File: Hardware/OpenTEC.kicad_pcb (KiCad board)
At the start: 4 copper layers, 130 x 90 mm, 67 parts, among them J10 TEMP3, J11 TEC, J12 XH2.54, J13 XH2.54, J14 XH2.54, J15 XH2.54, J16 XH2.54, J17 XH2.54, J18 XH2.54, J19 XH2.54, J2 4P Screw Terminal, J20 XH2.54, J21 XH2.54, J22 XH2.54, J23 XH2.54, J24 XH2.54, J25 XH2.54, J26 XH2.54, J27 XH2.54, J3 10P JTAG/SWD, J4 LCD, J5 I2C, J6 BOOT_SEL, J7 TEMP0, J8 TEMP1, J9 TEMP2, Q1 FDS6574A, Q2 FDS6574A, Q3 FDS6574A, Q4 FDS6574A, U11 STM32F103C8T6, U2 AMS1117-3.3, U3 IR2104, U4 IR2104, Y1 16MHz

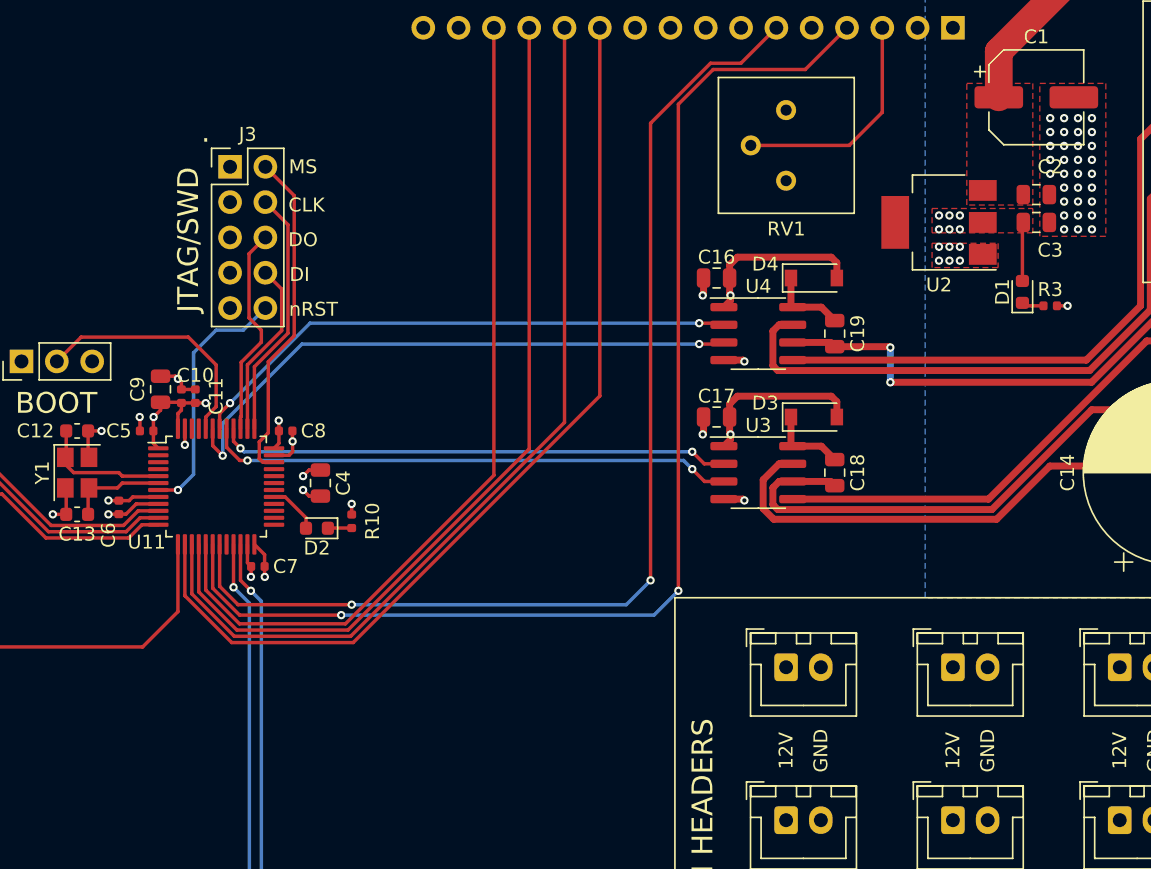
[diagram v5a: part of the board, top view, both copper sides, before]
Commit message: Add control push buttons
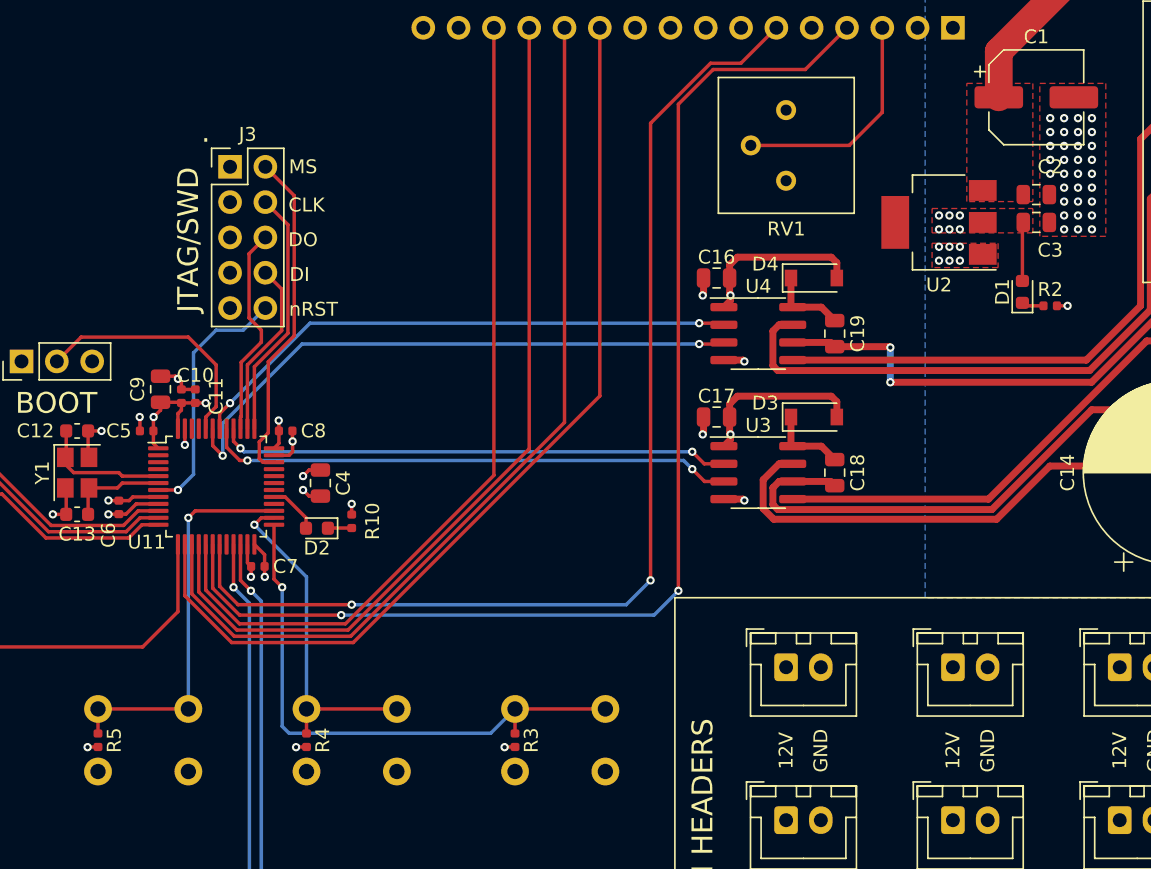
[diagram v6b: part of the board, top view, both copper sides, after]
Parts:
- added R3: 2.2K, Resistor_SMD:R_0402_1005Metric, F.Cu at (124.5, 112.2)
- added R4: 2.2K, Resistor_SMD:R_0402_1005Metric, F.Cu at (109.5, 112.2)
- added R5: 2.2K, Resistor_SMD:R_0402_1005Metric, F.Cu at (94.5, 112.2)
- added SW1: SW_Left, Button_Switch_THT:SW_PUSH_6mm, B.Cu at (131.0, 110.0)
- added SW2: SW_Mid, Button_Switch_THT:SW_PUSH_6mm, B.Cu at (116.0, 110.0)
- added SW3: SW_Right, Button_Switch_THT:SW_PUSH_6mm, B.Cu at (101.0, 110.0)
- renumbered R3 to R2
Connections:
- U11 pad 25: Net-(U11-Pad25) -> SW_Left
- U11 pad 26: Net-(U11-Pad26) -> SW_Mid
- U11 pad 27: Net-(U11-Pad27) -> SW_Right
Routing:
- net SW_Left: track 0.00 -> 40.7 mm, vias 0 -> 1
- net SW_Right: track 0.00 -> 28.4 mm, vias 0 -> 1
- net SW_Mid: track 0.00 -> 24.7 mm, vias 0 -> 1
- net GND: track 28.8 -> 31.1 mm, vias 95 -> 98

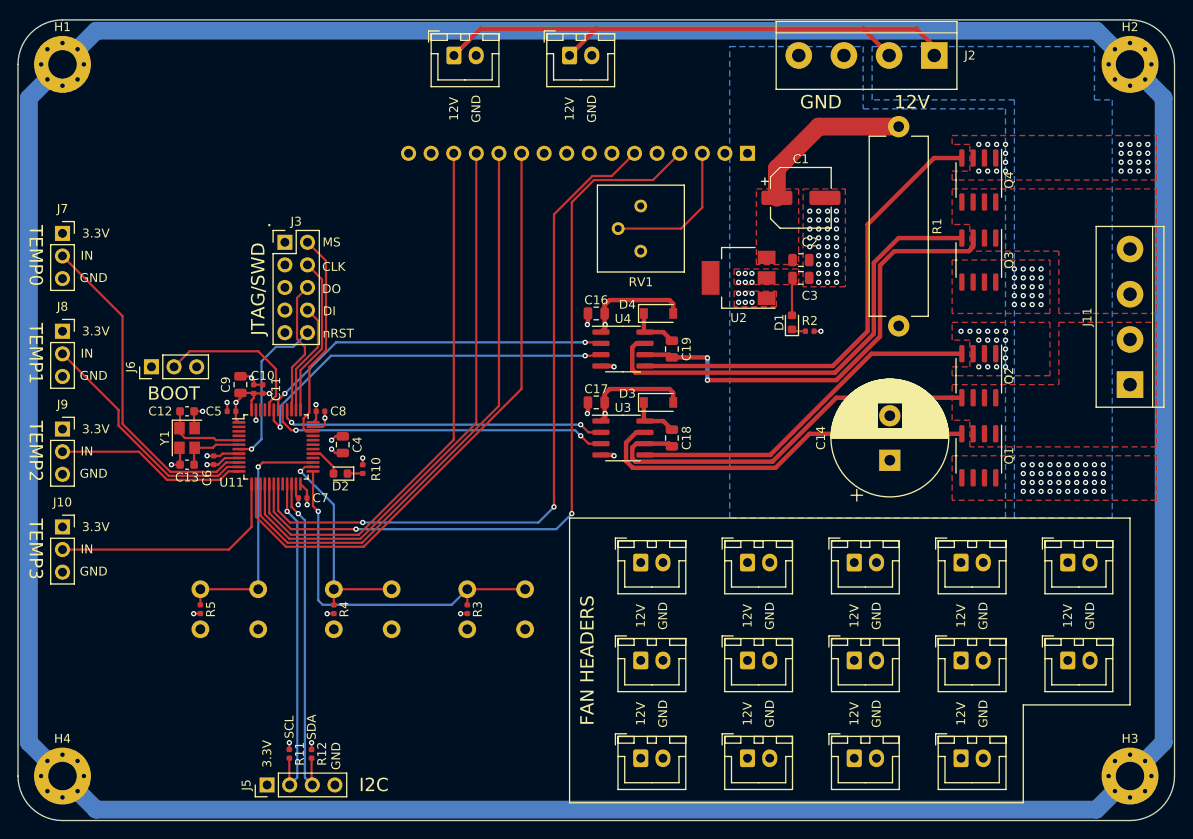
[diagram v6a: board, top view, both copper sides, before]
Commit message: Fix H-bridge supply voltage
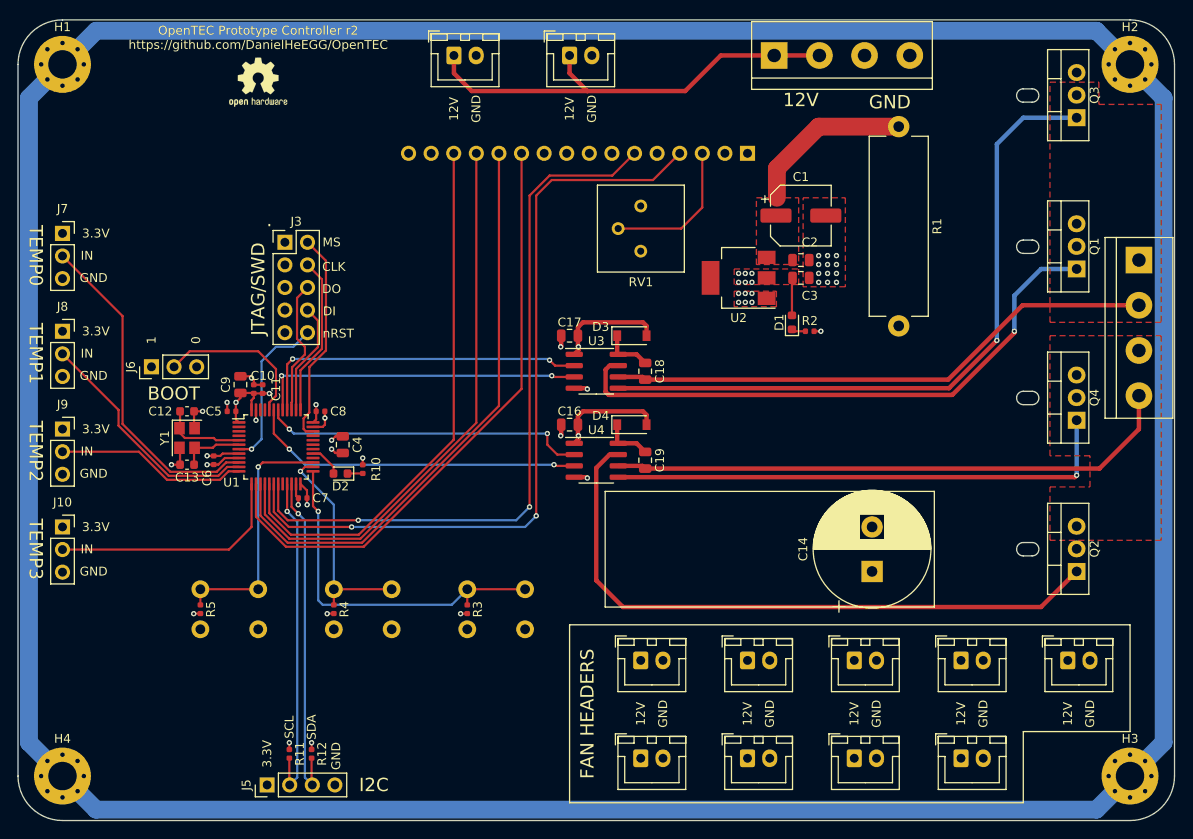
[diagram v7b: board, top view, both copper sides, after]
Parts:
- removed J23, J24, J25, J26, J27: XH2.54, Connector_JST:JST_XH_B2B-XH-A_1x02_P2.50mm_Vertical
- added REF**: OSHW-Logo2_7.3x6mm_SilkScreen, Symbol:OSHW-Logo2_7.3x6mm_SilkScreen, F.Cu at (101.0, 53.0)
- C1: footprint Capacitor_SMD:CP_Elec_6.3x5.8 -> Capacitor_SMD:CP_Elec_6.3x5.3
- Q1, Q2, Q3, Q4: value FDS6574A -> IRL2703; footprint Package_SO:SOIC-8_3.9x4.9mm_P1.27mm -> Package_TO_SOT_THT:TO-220-3_Vertical
- moved J12 97.4 mm to (123.0, 50.0)
- moved J14 68.5 mm to (144.0, 118.0)
- moved J19 52.8 mm to (144.0, 129.0)
- moved Q4 29.2 mm to (193.0, 91.0), turned to 90 degrees
- moved Q2 24.6 mm to (193.0, 108.0), turned to 90 degrees
- moved Q1 23.7 mm to (193.0, 74.0), turned to 90 degrees
- moved Q3 19.4 mm to (193.0, 57.0), turned to 90 degrees
- moved J2 18.0 mm to (159.0, 50.0), turned to 0 degrees
- moved J15 16.3 mm to (156.0, 118.0)
- moved J16 16.3 mm to (168.0, 118.0)
- moved J17 16.3 mm to (180.0, 118.0)
- moved J18 16.3 mm to (192.0, 118.0)
- moved J20 16.3 mm to (156.0, 129.0)
- moved J21 16.3 mm to (168.0, 129.0)
- moved J22 16.3 mm to (180.0, 129.0)
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- renumbered U11 to U1
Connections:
- C16 pad 1: +3V3 -> +12V
- C17 pad 1: +3V3 -> +12V
- D3 pad 2: +3V3 -> +12V
- D4 pad 2: +3V3 -> +12V
- Q1 pad 1: Net-(C18-Pad2) -> Net-(Q1-Pad1)
- Q1 pad 2: Net-(C18-Pad2) -> +12V
- Q2 pad 1: GND -> Net-(Q2-Pad1)
- Q2 pad 2: GND -> +12V
- Q2 pad 3: GND -> Net-(C19-Pad2)
- Q3 pad 1: Net-(C19-Pad2) -> Net-(Q3-Pad1)
- Q3 pad 2: Net-(C19-Pad2) -> Net-(C18-Pad2)
- Q3 pad 3: Net-(C19-Pad2) -> GND
- Q4 pad 1: GND -> Net-(Q4-Pad1)
- Q4 pad 2: GND -> Net-(C19-Pad2)
- U3 pad 1: +3V3 -> +12V
- U3 pad 5: Net-(Q2-Pad4) -> Net-(Q3-Pad1)
- U3 pad 7: Net-(Q1-Pad4) -> Net-(Q1-Pad1)
- U4 pad 1: +3V3 -> +12V
- U4 pad 5: Net-(Q4-Pad4) -> Net-(Q4-Pad1)
- U4 pad 7: Net-(Q3-Pad4) -> Net-(Q2-Pad1)
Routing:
- net Net-(Q3-Pad1): track 0.00 -> 77.0 mm, vias 0 -> 1
- net Net-(Q2-Pad1): track 0.00 -> 72.6 mm
- net Net-(Q1-Pad1): track 0.00 -> 65.5 mm, vias 0 -> 1
- net Net-(Q4-Pad1): track 0.00 -> 57.8 mm, vias 0 -> 1
- net Net-(Q4-Pad4): track 52.3 -> 0.00 mm
- net Net-(Q3-Pad4): track 52.2 -> 0.00 mm
- net Net-(Q1-Pad4): track 44.3 -> 0.00 mm
- net Net-(Q2-Pad4): track 40.3 -> 0.00 mm
- net +3V3: track 49.7 -> 24.8 mm, vias 16 -> 14
- net Net-(C18-Pad2): track 46.1 -> 62.1 mm
- net Net-(C19-Pad2): track 51.4 -> 64.2 mm, vias 2 -> 0
- net +12V: track 65.5 -> 75.3 mm, vias 60 -> 2
- net HB2_SD: track 43.0 -> 37.9 mm
- net HB2: track 40.1 -> 36.6 mm
- net HB1_SD: track 38.1 -> 36.8 mm
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- removed copper zone on B.Cu, net +12V
- removed copper zone on F.Cu, net +12V
- removed copper zone on B.Cu, net GND
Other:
- outline, holes or cut-outs redrawn
- board text added: "0"
- board text added: "1"
- board text added: "OpenTEC Prototype Controller r2 https://github.com/DanielHeEGG/OpenTEC"

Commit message: Add more vias to H-bridge
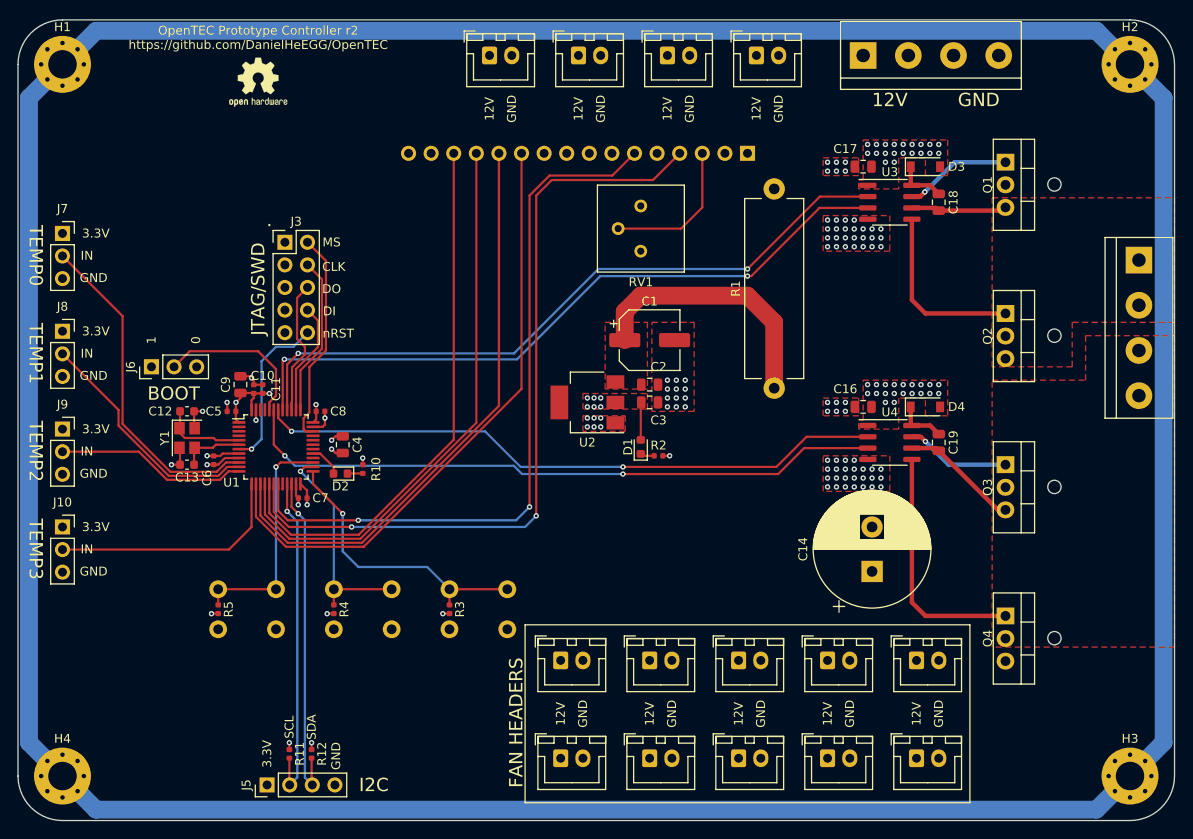
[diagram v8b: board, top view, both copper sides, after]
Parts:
- added J23: XH2.54, Connector_JST:JST_XH_B2B-XH-A_1x02_P2.50mm_Vertical, F.Cu at (137.0, 50.0)
- added J24: XH2.54, Connector_JST:JST_XH_B2B-XH-A_1x02_P2.50mm_Vertical, F.Cu at (147.0, 50.0)
- added J25: XH2.54, Connector_JST:JST_XH_B2B-XH-A_1x02_P2.50mm_Vertical, F.Cu at (157.0, 50.0)
- moved J22 95.1 mm to (127.0, 50.0)
- moved J12 69.1 mm to (135.0, 118.0)
- moved J13 68.6 mm to (145.0, 118.0)
- moved J18 48.3 mm to (145.0, 129.0)
- moved J17 46.3 mm to (135.0, 129.0)
- moved Q3 39.8 mm to (185.0, 96.0), turned to 270 degrees
- moved C17 38.1 mm to (169.0, 62.5)
- moved C18 38.1 mm to (177.5, 66.5)
- moved D3 38.1 mm to (176.0, 62.5)
- moved U3 38.1 mm to (172.0, 66.5)
- moved C16 33.1 mm to (169.0, 89.5)
- moved C19 33.1 mm to (177.5, 93.5)
- moved D4 33.1 mm to (176.0, 89.5)
- moved U4 33.1 mm to (172.0, 93.5)
- moved R1 32.6 mm to (159.0, 87.4), turned to 90 degrees
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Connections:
- Q2 pad 2: +12V -> Net-(C18-Pad2)
- Q2 pad 3: Net-(C19-Pad2) -> GND
- Q3 pad 2: Net-(C18-Pad2) -> +12V
- Q3 pad 3: GND -> Net-(C19-Pad2)
- U3 pad 5: Net-(Q3-Pad1) -> Net-(Q2-Pad1)
- U4 pad 7: Net-(Q2-Pad1) -> Net-(Q3-Pad1)
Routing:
- net +12V: track 75.3 -> 0.00 mm, vias 2 -> 40
- net Net-(Q3-Pad1): track 77.0 -> 11.8 mm
- net Net-(Q1-Pad1): track 65.5 -> 12.1 mm
- net Net-(Q2-Pad1): track 72.6 -> 20.2 mm
- net Net-(C18-Pad2): track 62.1 -> 10.8 mm
- net Net-(C19-Pad2): track 64.2 -> 13.4 mm
- net HB1_SD: track 36.8 -> 78.4 mm
- net HB1: track 37.9 -> 78.2 mm
- net HB2_SD: track 37.9 -> 73.3 mm
- net HB2: track 36.6 -> 70.9 mm
- net Net-(Q4-Pad1): track 57.8 -> 27.2 mm, vias 1 -> 0
- net Net-(C1-Pad1): track 18.9 -> 29.4 mm
- net SW_Left: track 40.7 -> 32.4 mm
- net GND: track 31.1 -> 25.5 mm, vias 36 -> 94
- net SW_Right: track 28.4 -> 26.4 mm
- added copper zone on F.Cu, net +12V
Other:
- outline, holes or cut-outs redrawn
